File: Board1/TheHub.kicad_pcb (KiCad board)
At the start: 2 copper layers, 195.6 x 195.6 mm, 67 parts, among them J1 ARM_ADC_1, J10 SCIENCE + WHEELS POWER CONN, J11 RFD900, J12 I2C_1 Test Point, J13 I2C_2 Test Point, J14 ARDUINO NANO LEFT, J15 GPIO Test, J16 I2C_3 Test Point, J17 12V OUT, J18 7.4V IN, J19 ANALOG SENSORS, J2 ARM_ADC_2, J20 GPS, J21 COMPASS, J22 ARDUINO NANO RIGHT, J23 NucleoRight, J3 ARM_PWM_OUT, J4 ARM POWER CONN, J5 NucleoLeft, J6 SCI_ADC_1, J7 SCIENCE_PWM_OUT, J8 12V MAIN POWER, J9 WHEEL_ADC_1, U1 PRE-PCA9685, U2 PRE-ADS1115, U3 PRE-ADS1115, U4 PRE-PCA9685, U5 PRE-ADS1115, U6 TL1963, U7 LM340MP-5.0, U9 PRE-ADS1115

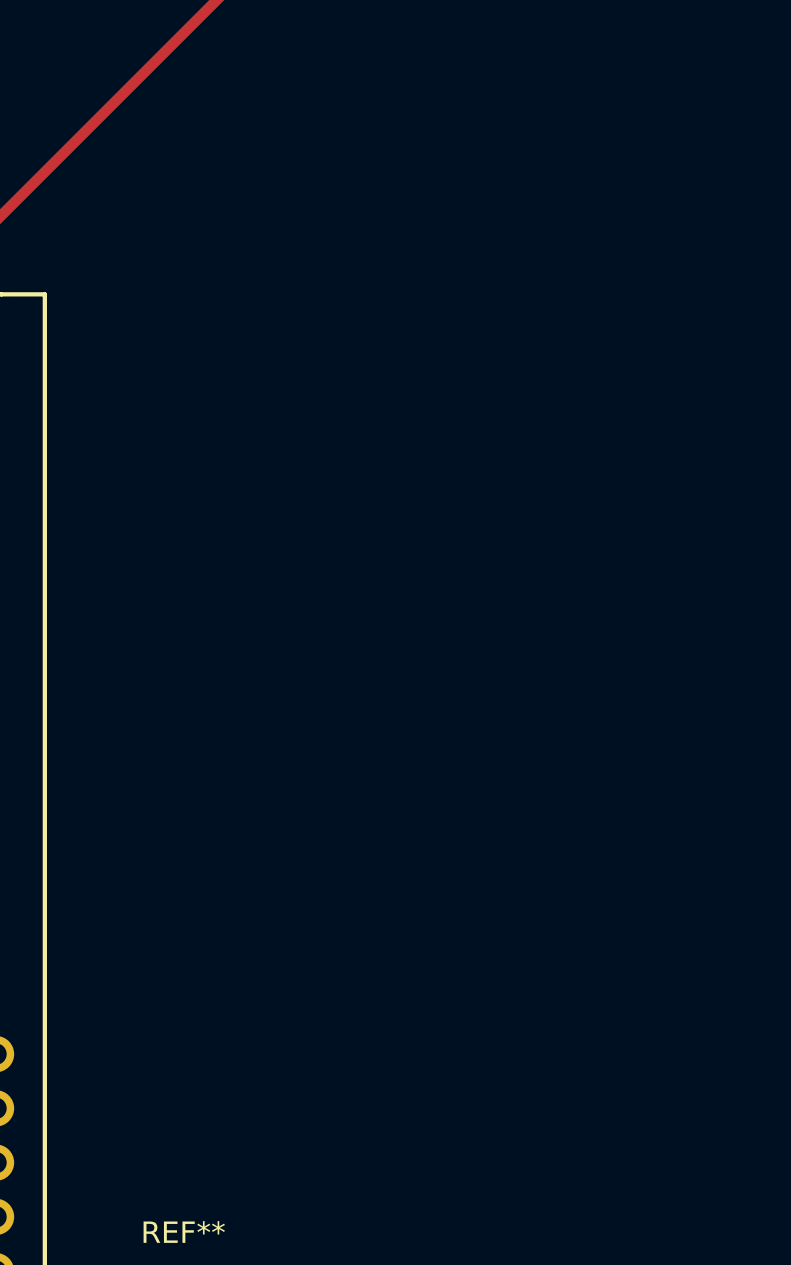
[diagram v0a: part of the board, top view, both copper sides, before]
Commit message: Add logo to PCB
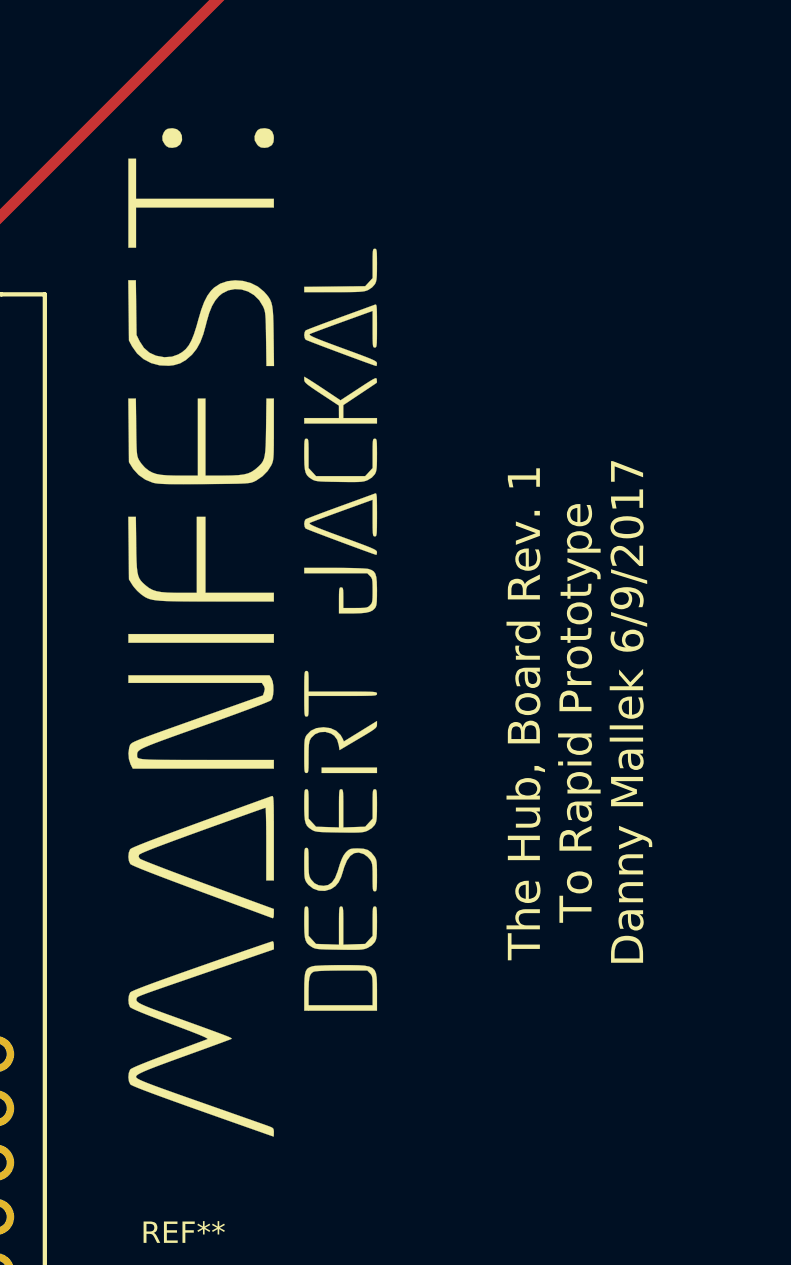
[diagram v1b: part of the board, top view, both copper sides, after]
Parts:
- added G***: LOGO, Board1:Logo1, F.Cu at (210.8, 198.1)
- added G***: LOGO, Board1:Logo1, B.Cu at (109.2, 144.1)
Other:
- board text added: "The Hub, Board Rev. 1 To Rapid Prototype Danny Mallek 6/9/2017"
